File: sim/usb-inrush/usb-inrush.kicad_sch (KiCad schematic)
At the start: 21 parts, among them K1 SMPS, U1 ${SIM.PARAMS}, U2 ${SIM.PARAMS}

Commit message: Started to draw the USB / power input module.
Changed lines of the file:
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@@
       (effects (font (size 1.27 1.27)) hide)
     )
-    (property "Sim.Params" "y1=0 y2=5 td=10m tr=20m tf=3m tw=1 per=1 np=1" (at 38.862 175.0144 0)
+    (property "Sim.Params" "y1=0 y2=5 td=15m tr=20m tf=3m tw=1 per=1 np=1" (at 38.862 175.0144 0)
       (effects (font (size 1.27 1.27)) (justify left))
     )

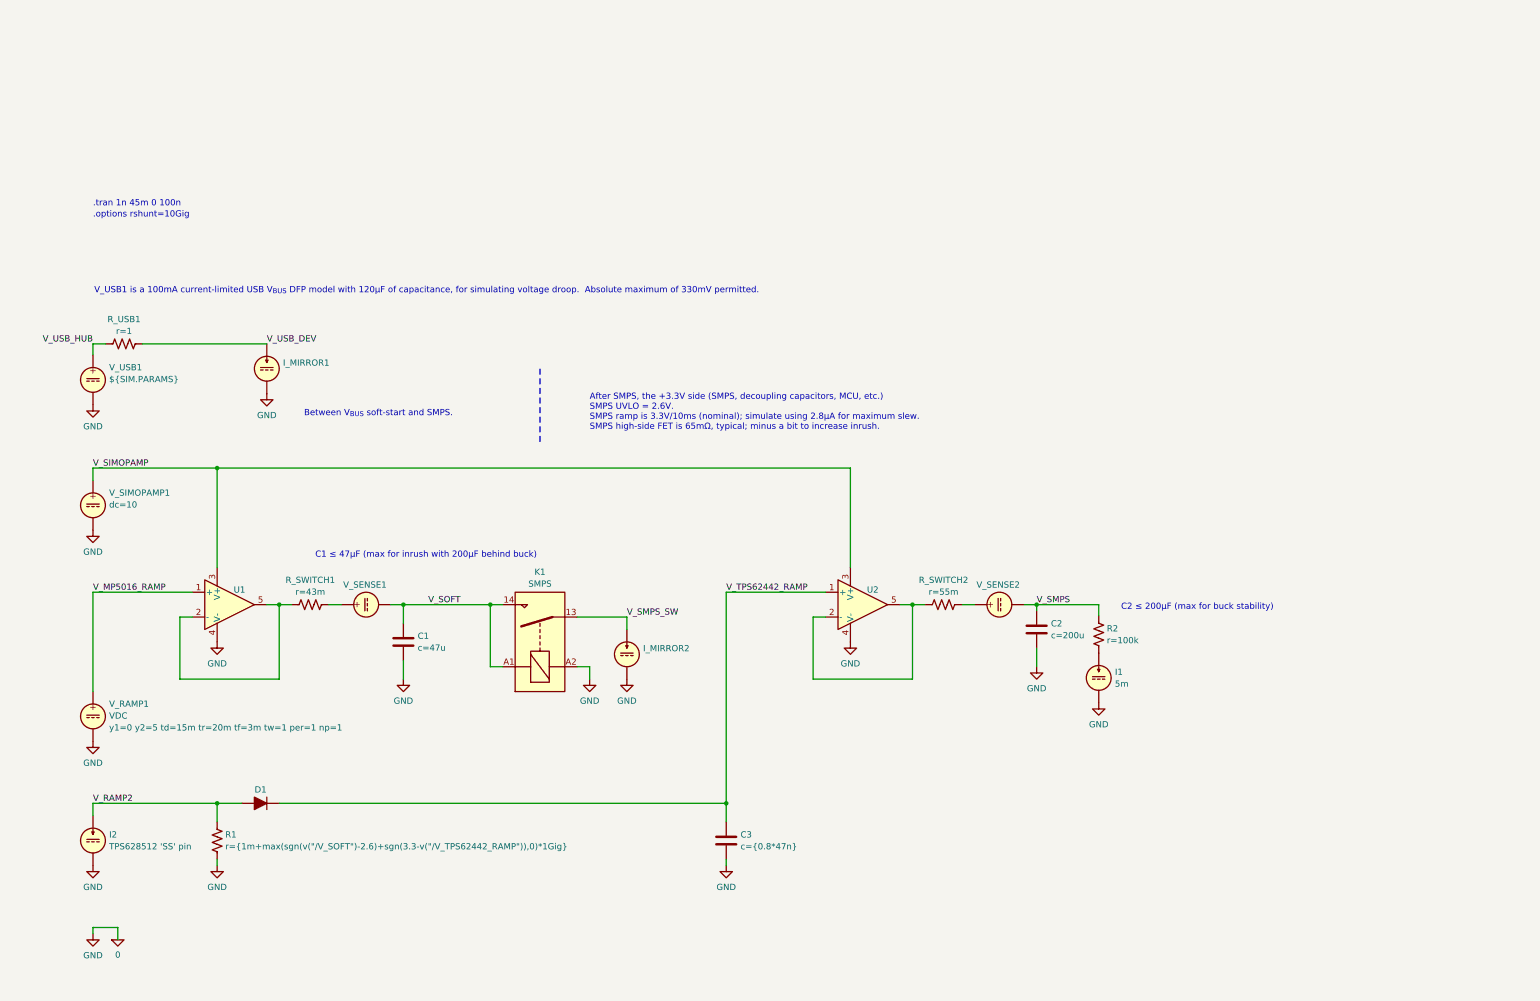
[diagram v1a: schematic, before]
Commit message: Further elaboration of the USB / Power schematic.
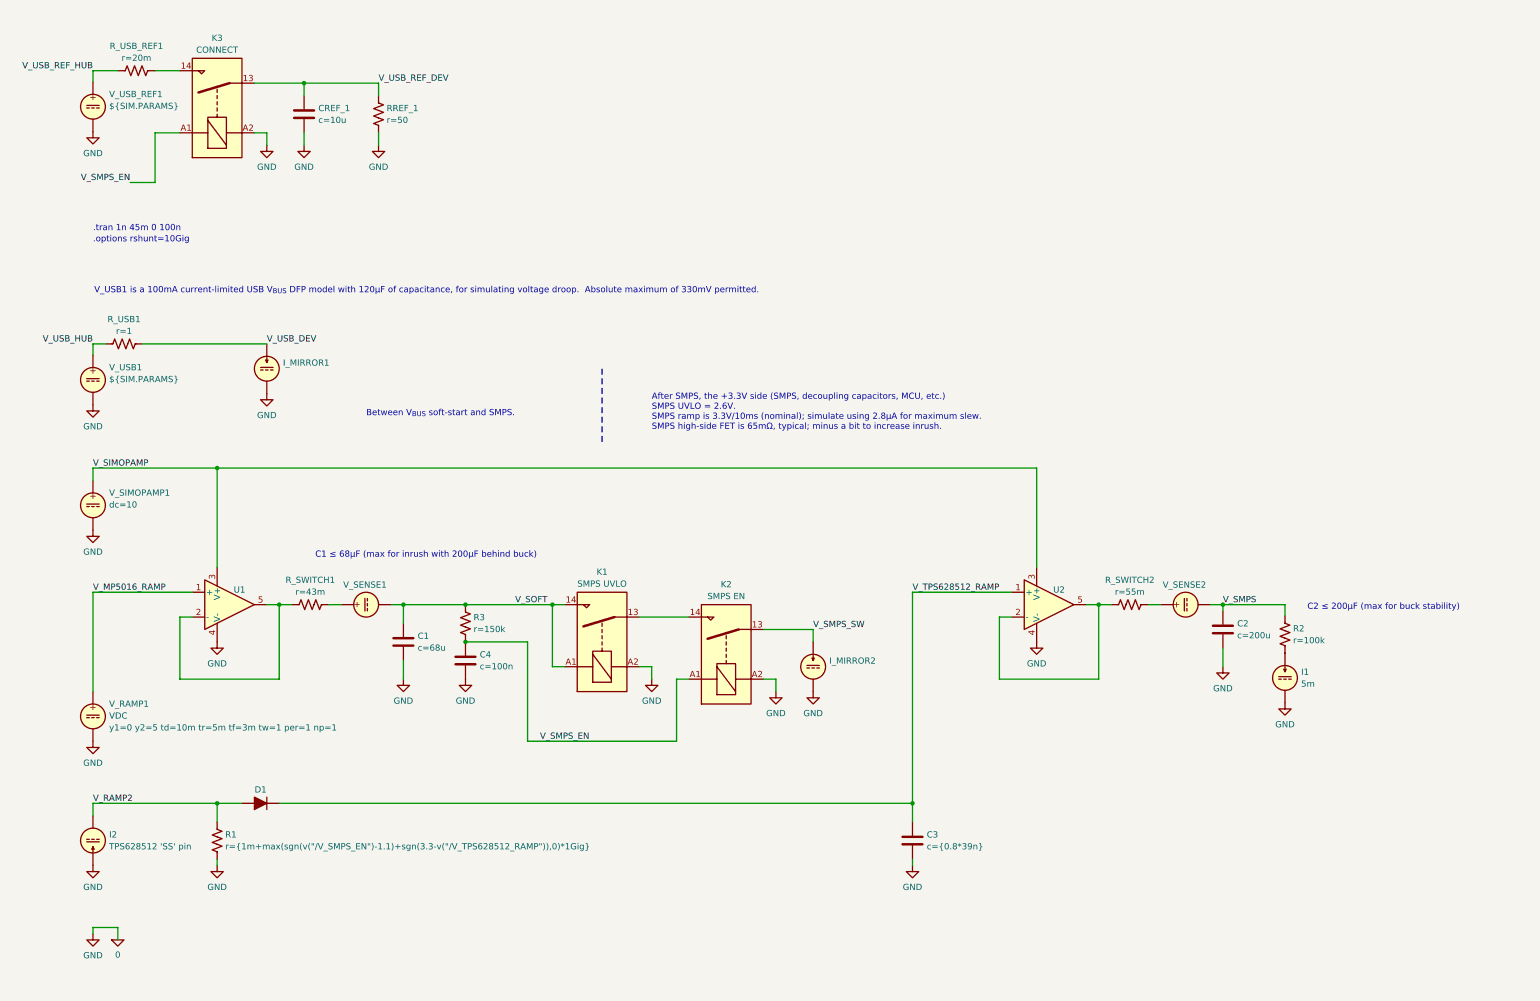
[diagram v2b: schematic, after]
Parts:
- added C4, CREF_1: ${SIM.PARAMS}, restall-generic-capacitors:unpolarised-nominal-0402-1005, symbol restall-generic-capacitors:capacitor-unpolarised
- added K2: SMPS EN, symbol Relay:Relay_SPST-NO
- added K3: CONNECT, symbol Relay:Relay_SPST-NO
- added R3, RREF_1, R_USB_REF1: ${SIM.PARAMS}, restall-generic-resistors:nominal-0402-1005, symbol restall-generic-resistors:resistor
- added V_USB_REF1: ${SIM.PARAMS}, symbol Simulation_SPICE:VDC
- K1: value SMPS -> SMPS UVLO
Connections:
- net 0: now also I2.1, C4.2, CREF_1.2, K2.A2, K3.A2, RREF_1.1, V_USB_REF1.2; no longer I2.2
- net V_RAMP2: now also I2.2; no longer I2.1
- net V_SMPS_SW: now also K2.13; no longer K1.13
- net V_SOFT: now also R3.2
- net V_TPS62442_RAMP renamed V_TPS628512_RAMP
- new net: K1.13, K2.14
- new net: K3.14, R_USB_REF1.2
- new net V_SMPS_EN: C4.1, K2.A1, K3.A1, R3.1
- new net V_USB_REF_DEV: CREF_1.1, K3.13, RREF_1.2
- new net V_USB_REF_HUB: R_USB_REF1.1, V_USB_REF1.1
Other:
- note added: "C1 ≤ 68μF (max for inrush with 200μF behind buck)"
- note removed: "C1 ≤ 47μF (max for inrush with 200μF behind buck)"
- moved on the sheet: C2, C3, I1, I_MIRROR2, K1, R2, R_SWITCH2, U2, V_SENSE2

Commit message: Initial stab at a simulation for the buck regulator.  Started to flesh out the USB / power schematics.  More work required to figure out the large ripple on the buck regulator's input, which looks to be related to the ESL of the input capacitors.
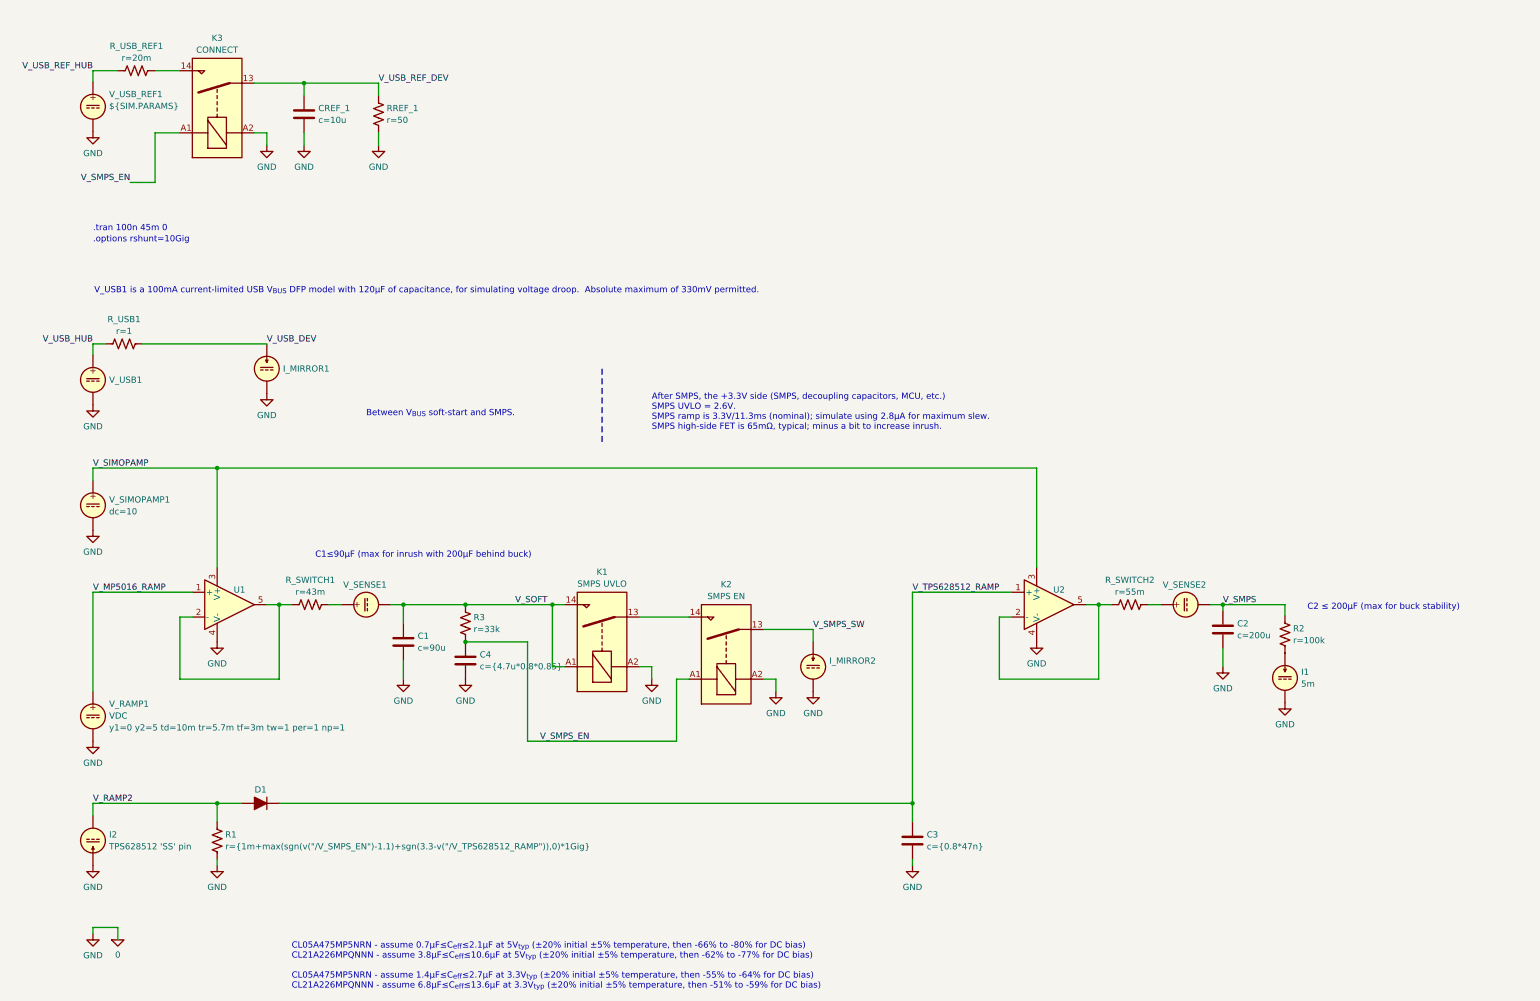
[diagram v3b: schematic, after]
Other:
- note added: ".tran 100n 45m 0"
- note added: "After SMPS, the +3.3V side (SMPS, decoupling capacitors, MCU, etc.) SMPS UVLO = 2.6V. SMPS ramp is 3.3V/11.3ms (nominal); simulate using 2.8μA for maximum slew. SMPS high-side FET is 65mΩ, typical; minus a bit to increase inrush."
- note added: "C1≤90μF (max for inrush with 200μF behind buck)"
- note added: "CL05A475MP5NRN - assume 0.7μF≤C_{eff}≤2.1μF at 5V_{typ} (±20% initial ±5% temperature, then -66% to -80% for DC bias) CL21A226MPQNNN - assume 3.8μF≤C_{eff}≤10.6μF at 5V_{typ} (±20% initial ±5% temperature, then -62% to -77% for DC bias) CL05A475MP5NRN - assume 1.4μF≤C_{eff}≤2.7μF at 3.3V_{typ} (±20% initial ±5% temperature, then -55% to -64% for DC bias) CL21A226MPQNNN - assume 6.8μF≤C_{eff}≤13.6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"
- note removed: ".tran 1n 45m 0 100n"
- note removed: "After SMPS, the +3.3V side (SMPS, decoupling capacitors, MCU, etc.) SMPS UVLO = 2.6V. SMPS ramp is 3.3V/10ms (nominal); simulate using 2.8μA for maximum slew. SMPS high-side FET is 65mΩ, typical; minus a bit to increase inrush."
- note removed: "C1 ≤ 68μF (max for inrush with 200μF behind buck)"
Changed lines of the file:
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@@
     (effects (font (size 1.27 1.27)) (justify left bottom))
   )
-  (text "C1 ≤ 68μF (max for inrush with 200μF behind buck)" (at 81.026 140.462 0)
+  (text "CL05A475MP5NRN - assume 0.7μF≤C_{eff}≤2.1μF at 5V_{typ} (±20% initial ±5% temperature, then -66% to -80% for DC bias)\nCL21A226MPQNNN - assume 3.8μF≤C_{eff}≤10.6μF at 5V_{typ} (±20% initial ±5% temperature, then -62% to -77% for DC bias)\n\nCL05A475MP5NRN - assume 1.4μF≤C_{eff}≤2.7μF at 3.3V_{typ} (±20% initial ±5% temperature, then -55% to -64% for DC bias)\nCL21A226MPQNNN - assume 6.8μF≤C_{eff}≤13.6μF at 3.3V_{typ} (±20% initial ±5% temperature, then -51% to -59% for DC bias)"
+    (at 76.2 228.6 0)
     (effects (font (size 1.27 1.27)) (justify left bottom))
   )
-  (text ".tran 1n 45m 0 100n" (at 35.56 73.66 0)
+  (text "C1≤90μF (max for inrush with 200μF behind buck)" (at 81.026 140.462 0)
+    (effects (font (size 1.27 1.27)) (justify left bottom))
+  )
+  (text ".tran 100n 45m 0" (at 35.56 73.66 0)
     (effects (font (size 1.27 1.27)) (justify left bottom))
   )
@@
     (effects (font (size 1.27 1.27)) (justify left bottom))
   )
-  (text "After SMPS, the +3.3V side (SMPS, decoupling capacitors, MCU, etc.)\nSMPS UVLO = 2.6V.\nSMPS ramp is 3.3V/10ms (nominal); simulate using 2.8μA for maximum slew.\nSMPS high-side FET is 65mΩ, typical; minus a bit to increase inrush."
+  (text "After SMPS, the +3.3V side (SMPS, decoupling capacitors, MCU, etc.)\nSMPS UVLO = 2.6V.\nSMPS ramp is 3.3V/11.3ms (nominal); simulate using 2.8μA for maximum slew.\nSMPS high-side FET is 65mΩ, typical; minus a bit to increase inrush."
     (at 149.86 114.3 0)
     (effects (font (size 1.27 1.27)) (justify left bottom))
@@
   )
   (symbol (lib_id "Simulation_SPICE:VDC") (at 35.56 129.54 0) (unit 1)
-    (in_bom yes) (on_board yes) (dnp no) (fields_autoplaced)
-    (property "Reference" "V_SIMOPAMP1" (at 38.862 126.986 0)
-      (effects (font (size 1.27 1.27)) (justify left))
-    )
-    (property "Value" "${SIM.PARAMS}" (at 38.862 129.4102 0)
+    (in_bom yes) (on_board yes) (dnp no)
+    (property "Reference" "V_SIMOPAMP1" (at 38.862 128.3858 0)
+      (effects (font (size 1.27 1.27)) (justify left))
+    )
+    (property "Value" "${SIM.PARAMS}" (at 38.862 130.81 0)
       (effects (font (size 1.27 1.27)) (justify left))
     )
@@
       (effects (font (size 1.27 1.27)) hide)
     )
-    (property "Sim.Params" "c={0.8*39n}" (at 203.2 198.12 0)
+    (property "Sim.Params" "c={0.8*47n}" (at 203.2 198.12 0)
       (effects (font (size 1.27 1.27)) hide)
     )
@@
   )
   (symbol (lib_id "Simulation_SPICE:VDC") (at 35.56 103.886 0) (unit 1)
-    (in_bom yes) (on_board yes) (dnp no) (fields_autoplaced)
-    (property "Reference" "V_USB1" (at 38.862 101.332 0)
+    (in_bom yes) (on_board yes) (dnp no)
+    (property "Reference" "V_USB1" (at 38.862 103.886 0)
       (effects (font (size 1.27 1.27)) (justify left))
     )
     (property "Value" "${SIM.PARAMS}" (at 38.862 103.7562 0)
-      (effects (font (size 1.27 1.27)) (justify left))
+      (effects (font (size 1.27 1.27)) (justify left) hide)
     )
     (property "Footprint" "" (at 35.56 103.886 0)
@@
       (effects (font (size 1.27 1.27)) hide)
     )
-    (property "Sim.Params" "c=100n" (at 111.76 161.29 0)
+    (property "Sim.Params" "c={4.7u*0.8*0.85}" (at 111.76 161.29 0)
       (effects (font (size 1.27 1.27)) hide)
     )
@@
   )
   (symbol (lib_id "Simulation_SPICE:IDC") (at 71.12 101.6 0) (unit 1)
-    (in_bom yes) (on_board yes) (dnp no) (fields_autoplaced)
-    (property "Reference" "I_MIRROR1" (at 74.422 100.3879 0)
+    (in_bom yes) (on_board yes) (dnp no)
+    (property "Reference" "I_MIRROR1" (at 74.422 101.6 0)
       (effects (font (size 1.27 1.27)) (justify left))
     )
@@
       (effects (font (size 1.27 1.27)) hide)
     )
-    (property "Sim.Params" "r=150k" (at 187.96 218.44 0)
+    (property "Sim.Params" "r=33k" (at 187.96 218.44 0)
       (effects (font (size 1.27 1.27)) hide)
     )
@@
       (effects (font (size 1.27 1.27)) hide)
     )
-    (property "Sim.Params" "y1=0 y2=5 td=10m tr=5m tf=3m tw=1 per=1 np=1" (at 38.862 175.0144 0)
+    (property "Sim.Params" "y1=0 y2=5 td=10m tr=5.7m tf=3m tw=1 per=1 np=1" (at 38.862 175.0144 0)
       (effects (font (size 1.27 1.27)) (justify left))
     )
@@
       (effects (font (size 1.27 1.27)) hide)
     )
-    (property "Sim.Params" "c=68u" (at 99.06 157.48 0)
-      (effects (font (size 1.27 1.27)) hide)
-    )
+    (property "Sim.Params" "c=90u" (at 99.06 157.48 0)
+      (effects (font (size 1.27 1.27)) hide)
+    )

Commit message: Various tidy-ups and checks, mainly around the bypass capacitors.  Added a load of test points.
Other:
- note added: "C2 ≤ 200μF (max for buck stability). Plus 25μF for the sensors (behind an LDO regulator so affects the inrush but isolates from the buck)."
- note added: "Reference waveforms, per USB specification."
- note removed: "C2 ≤ 200μF (max for buck stability)"
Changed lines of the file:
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@@
     (effects (font (size 1.27 1.27)) (justify left bottom))
   )
-  (text "C2 ≤ 200μF (max for buck stability)" (at 283.972 151.13 0)
+  (text "Reference waveforms, per USB specification." (at 43.18 30.48 0)
+    (effects (font (size 1.27 1.27)) (justify left bottom))
+  )
+  (text "C2 ≤ 200μF (max for buck stability).\nPlus 25μF for the sensors (behind\nan LDO regulator so affects the\ninrush but isolates from the buck)."
+    (at 283.972 151.13 0)
     (effects (font (size 1.27 1.27)) (justify left bottom))
   )
@@
       (effects (font (size 1.27 1.27)) hide)
     )
-    (property "Sim.Params" "c=200u" (at 266.7 154.94 0)
-      (effects (font (size 1.27 1.27)) hide)
-    )
+    (property "Sim.Params" "c=225u" (at 266.7 154.94 0)
+      (effects (font (size 1.27 1.27)) hide)
+    )
